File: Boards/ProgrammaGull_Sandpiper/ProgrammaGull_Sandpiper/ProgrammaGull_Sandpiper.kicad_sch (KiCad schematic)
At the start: 194 parts, among them J4 Conn_01x22_Socket, P1 USB_C_Plug_USB2.0, Q1 MMBT2907, Q2 MMBT2907, Q3 MMBT2907, Q4 MMBT2907, Q5 MMBT2907, Q6 MMBT2907, Q7 MMBT2907, Q8 MMBT2907, SW10 SW_Push, SW11 SW_Push, SW12 SW_Push, SW13 SW_Push, SW14 SW_Push, SW15 RotaryEncoder, SW9 SW_Push, U1 ICE40UP5K-SG48ITR, U11 ADC084S051CIMM/NOPB, U12 74HC596, U13 74AHC595, U14 W25Q32JVSS, U15 AMS1117-3.3, U2 SN74LVC1G126DCKR, U4 MIC5504-1.2YM5, U5 MIC5504-2.5YM5, U6 93LCxxAxxOT, U7 FT2232HQ, U9 74AHC595, X1 SG-210STF

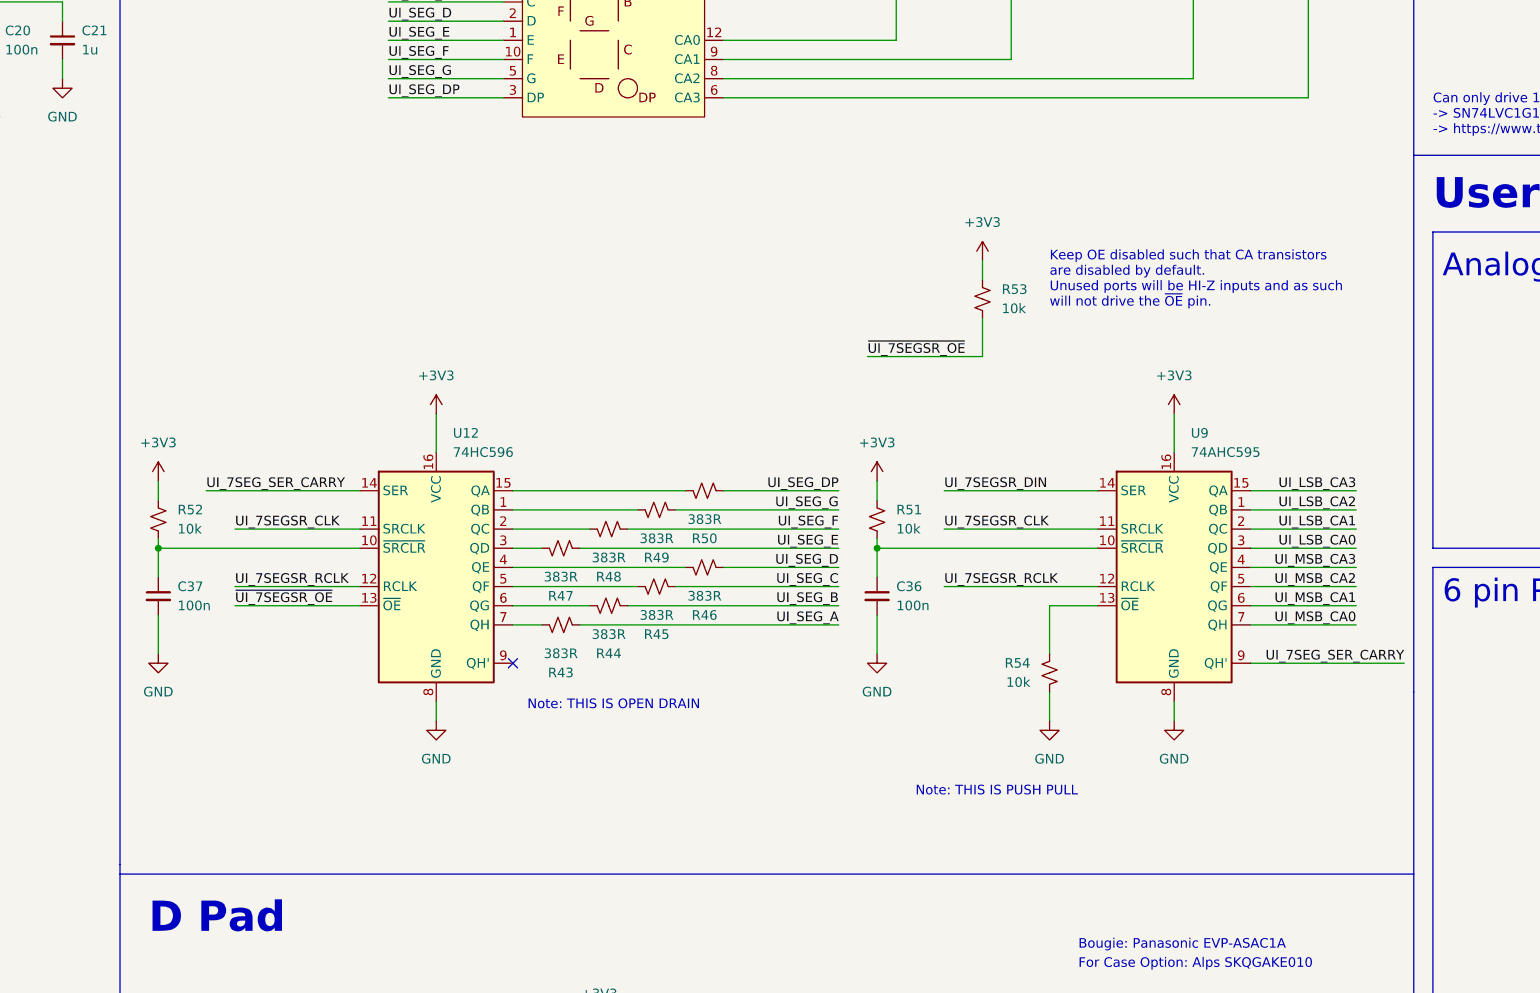
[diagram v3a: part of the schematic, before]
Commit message: Fixed 7 segment drive circuitry to work properly, swap to 74 596 + segment brightness limiting resistors
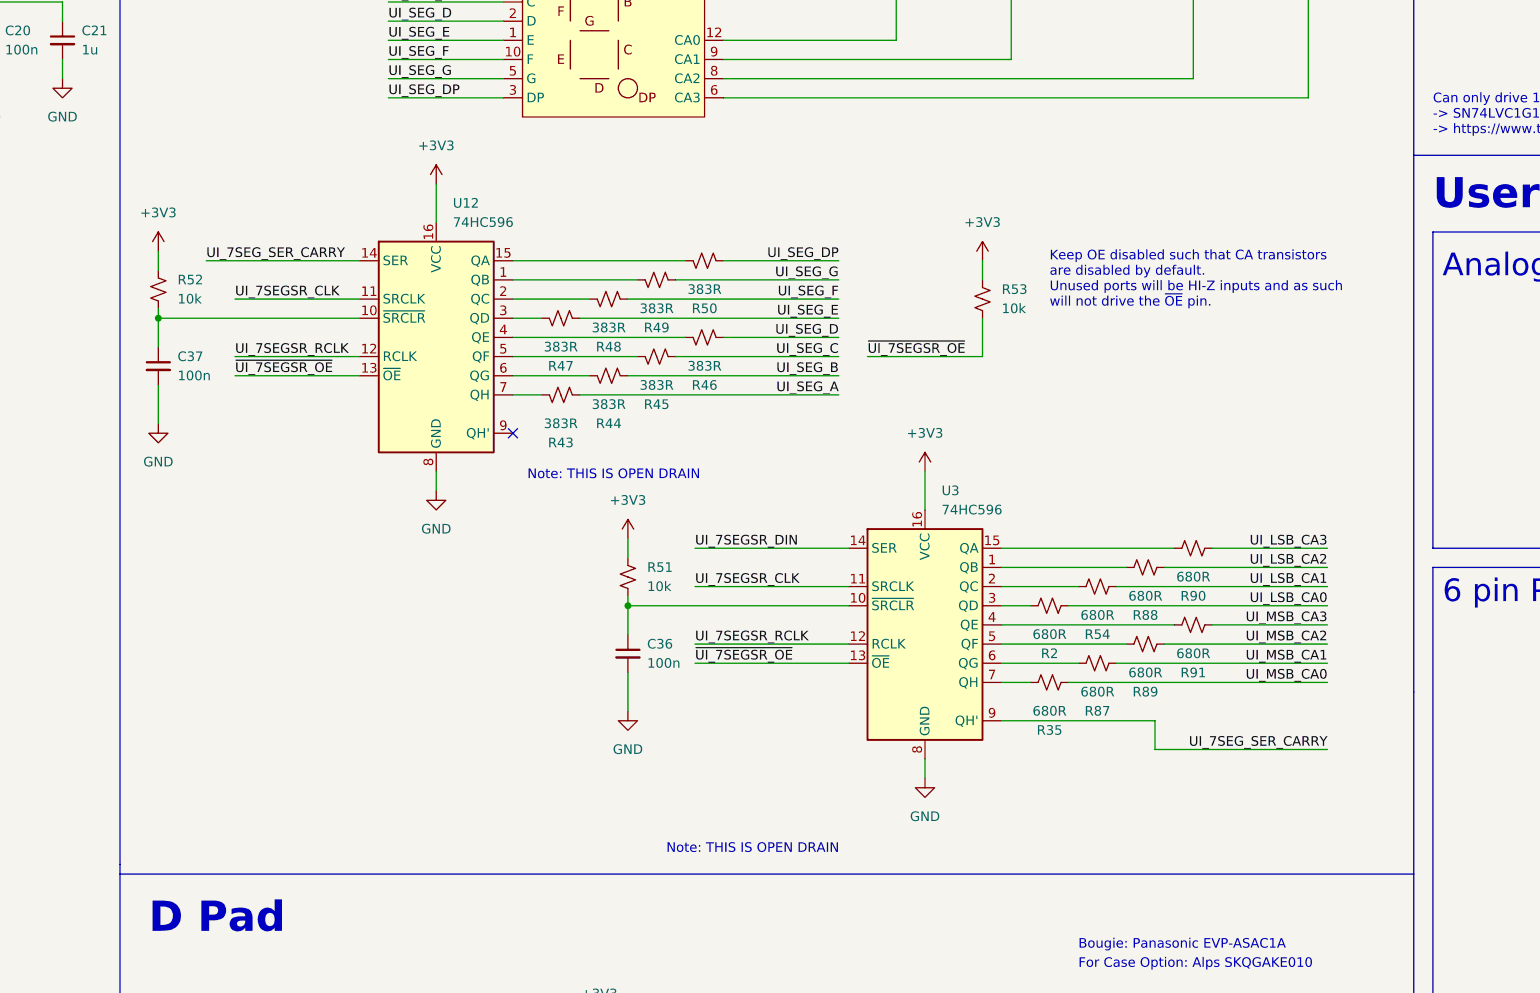
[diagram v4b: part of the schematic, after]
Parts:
- removed U9: 74AHC595, Package_SO:TSSOP-16_4.4x5mm_P0.65mm, symbol 74xx:74AHC595
- added R2, R35, R87, R88, R89, R90, R91: 680R, Resistor_SMD:R_0603_1608Metric, symbol Device:R_Small_US
- added U3: 74HC596, Package_SO:TSSOP-16_4.4x5mm_P0.65mm, symbol 74xx:74HC596
- R54: value 10k -> 680R
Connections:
- net +3V3: now also U3.16 (VCC)
- net GND: now also U3.8 (GND); no longer R54.1
- net UI_7SEGSR_CLK: now also U3.11 (SRCLK)
- net UI_7SEGSR_DIN: now also U3.14 (SER)
- net UI_7SEGSR_RCLK: now also U3.12 (RCLK)
- net UI_7SEG_SER_CARRY: now also U3.9 (QH')
- net UI_LSB_CA0: now also R2.1
- net UI_LSB_CA1: now also R54.1
- net UI_LSB_CA2: now also R88.1
- net UI_LSB_CA3: now also R90.1
- net UI_MSB_CA0: now also R35.1
- net UI_MSB_CA1: now also R87.1
- net UI_MSB_CA2: now also R89.1
- net UI_MSB_CA3: now also R91.1
- net ~{UI_7SEGSR_OE}: now also U3.13 (~{OE})
- net at R54.2: now also U3.2 (QC)
- net at C36.1, R51.1: now also U3.10 (~{SRCLR})
- new net: R35.2, U3.7 (QH)
- new net: R89.2, U3.5 (QF)
- new net: R90.2, U3.15 (QA)
- new net: R87.2, U3.6 (QG)
- new net: R2.2, U3.3 (QD)
- new net: R88.2, U3.1 (QB)
- new net: R91.2, U3.4 (QE)
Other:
- note removed: "Note: THIS IS PUSH PULL"
- moved on the sheet: C36, C37, R43, R44, R45, R46, R47, R48, R49, R50, R51, R52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

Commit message: Adjustments made to better fit JLC/LCSC Parts Library
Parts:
- removed C38, C39: 100n, Capacitor_SMD:C_0603_1608Metric, symbol Device:C_Small
- removed C7: 10u, Capacitor_SMD:C_0805_2012Metric, symbol Device:C_Small
- removed R30, R75, R78: 10k, Resistor_SMD:R_0603_1608Metric, symbol Device:R_Small_US
- removed R31: 220R, Resistor_SMD:R_0603_1608Metric, symbol Device:R_Small_US
- removed R76, R77: 2k2, Resistor_SMD:R_0603_1608Metric, symbol Device:R_Small_US
- removed SW13: SW_Push, ProgrammaGull_Logic:Alps_SKQGAKE010, symbol Switch:SW_Push
- removed SW15: RotaryEncoder, Rotary_Encoder:RotaryEncoder_Bourns_Vertical_PEC12R-3xxxF-Nxxxx, symbol Device:RotaryEncoder
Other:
- note added: "Center Button in Rev 2!"
- note added: "Digi/Mouser: SLW-121586-5A-D LCSC Alternate: SS12F44G4 / C2887261"
- note added: "INCLUDED IN REV 2!!"
- note removed: "OUT OF PINS NO USEY"
